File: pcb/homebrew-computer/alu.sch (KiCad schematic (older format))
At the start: 8 parts

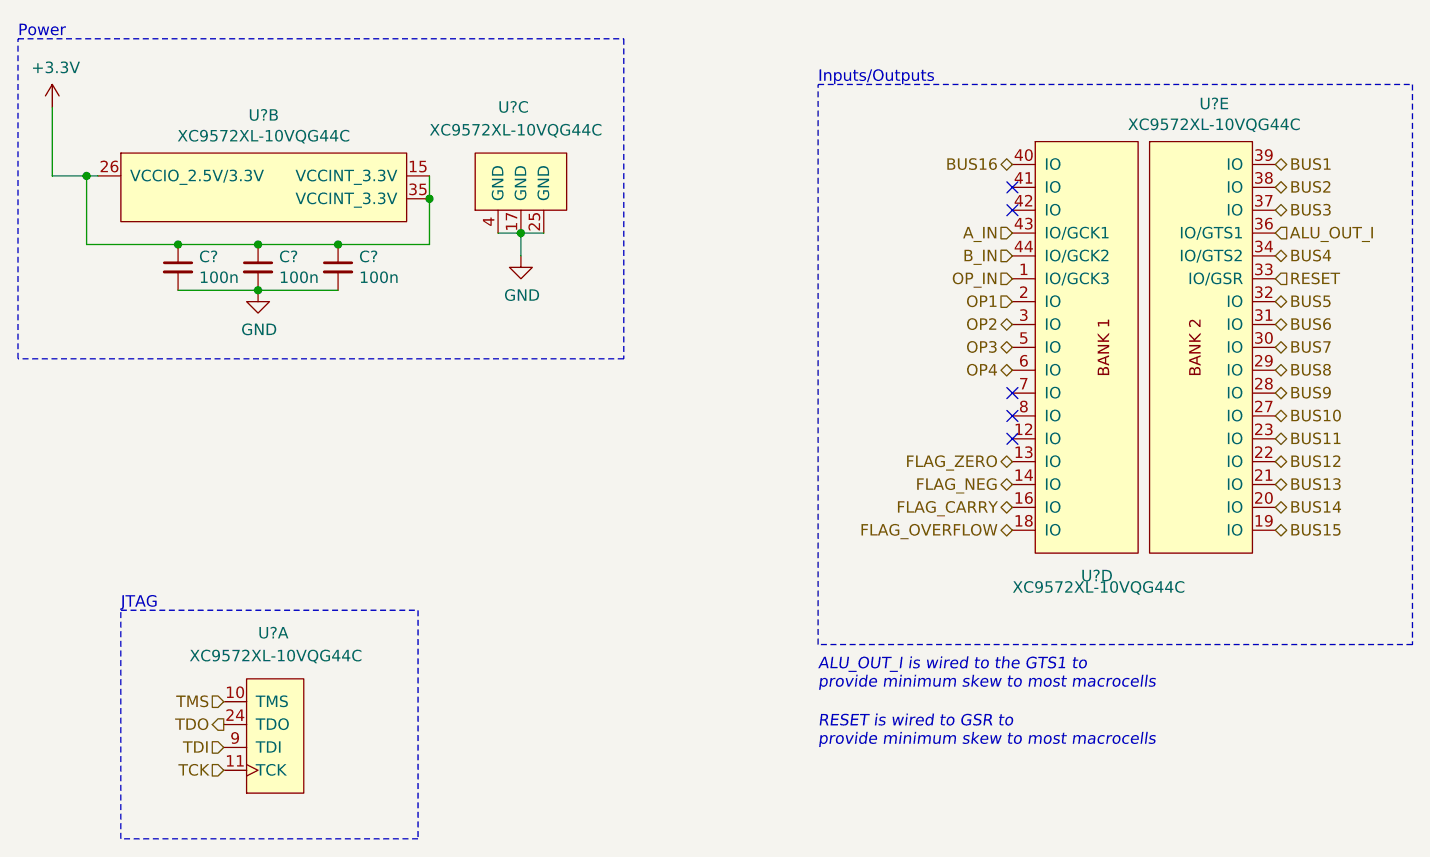
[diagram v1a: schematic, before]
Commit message: Start changing global labels with local labels
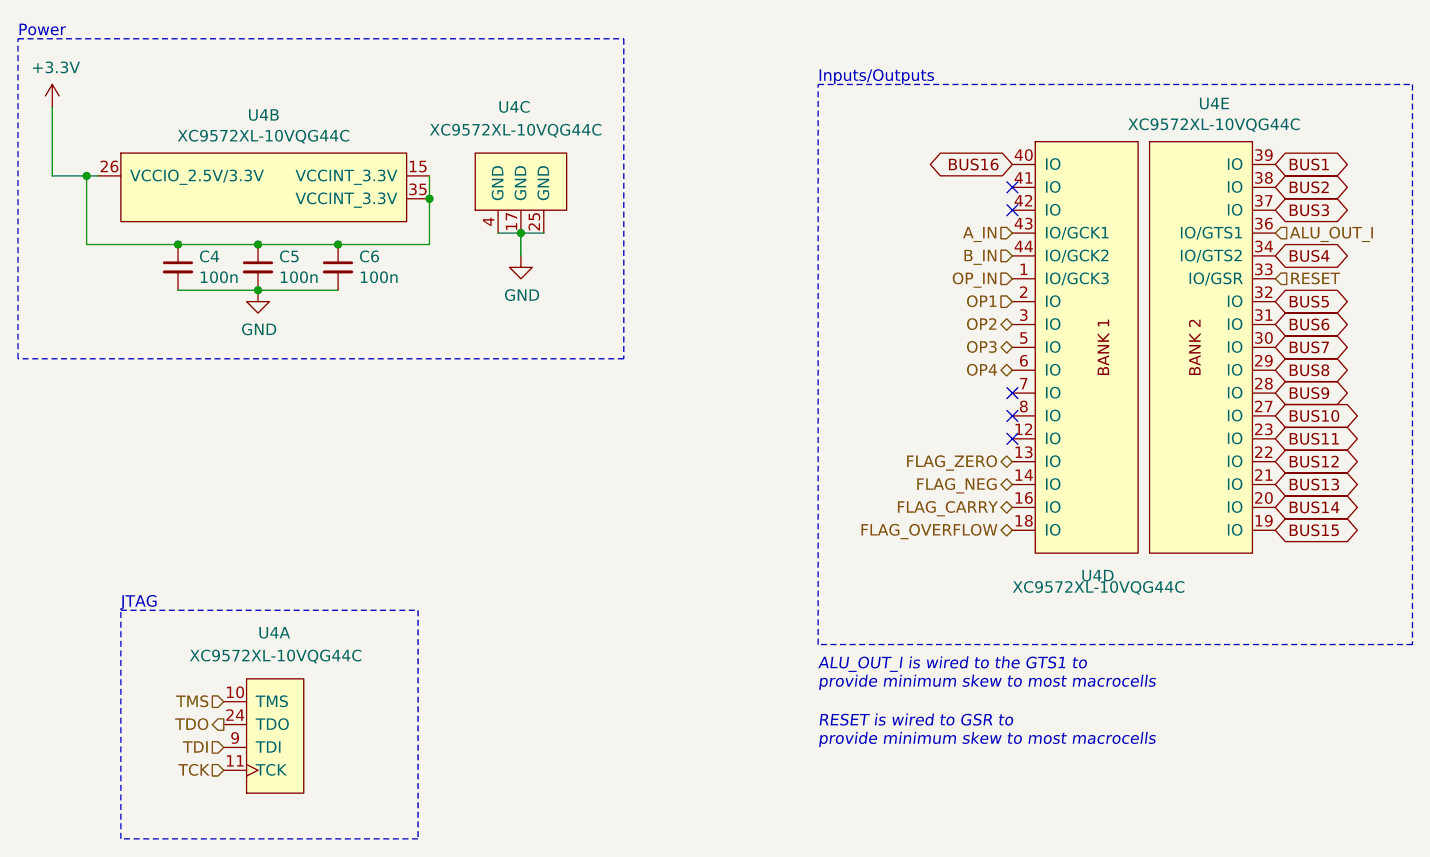
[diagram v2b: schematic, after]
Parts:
- gave numbers to parts that had none: 4
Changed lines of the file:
@@
 $Descr User 8661 5906
 encoding utf-8
-Sheet 2 7
+Sheet 5 7
 Title "Arithmetic and Logic Unit"
 Date "2020-10-24"
@@
 $EndComp
 $Comp
-L Device:C_Small C?
+L Device:C_Small C4
 U 1 1 5F8E42A8
 P 1700 1700
-F 0 "C?" H 1792 1746 50  0000 L CNN
+F 0 "C4" H 1792 1746 50  0000 L CNN
 F 1 "100n" H 1792 1655 50  0000 L CNN
 F 2 "" H 1700 1700 50  0001 C CNN
@@
 $EndComp
 $Comp
-L Device:C_Small C?
+L Device:C_Small C5
 U 1 1 5F8E4555
 P 2050 1700
-F 0 "C?" H 2142 1746 50  0000 L CNN
+F 0 "C5" H 2142 1746 50  0000 L CNN
 F 1 "100n" H 2142 1655 50  0000 L CNN
 F 2 "" H 2050 1700 50  0001 C CNN
@@
 $EndComp
 $Comp
-L Device:C_Small C?
+L Device:C_Small C6
 U 1 1 5F8E49E6
 P 2400 1700
-F 0 "C?" H 2492 1746 50  0000 L CNN
+F 0 "C6" H 2492 1746 50  0000 L CNN
 F 1 "100n" H 2492 1655 50  0000 L CNN
 F 2 "" H 2400 1700 50  0001 C CNN
@@
 Text HLabel 6500 1550 2    50   Input ~ 0
 ALU_OUT_I
-Text HLabel 6500 1250 2    50   3State ~ 0
-BUS1
-Text HLabel 6500 1350 2    50   3State ~ 0
-BUS2
-Text HLabel 6500 1450 2    50   3State ~ 0
-BUS3
-Text HLabel 6500 1650 2    50   3State ~ 0
-BUS4
-Text HLabel 6500 1850 2    50   3State ~ 0
-BUS5
-Text HLabel 6500 1950 2    50   3State ~ 0
-BUS6
-Text HLabel 6500 2050 2    50   3State ~ 0
-BUS7
-Text HLabel 6500 2150 2    50   3State ~ 0
-BUS8
-Text HLabel 6500 2250 2    50   3State ~ 0
-BUS9
-Text HLabel 6500 2350 2    50   3State ~ 0
-BUS10
-Text HLabel 6500 2450 2    50   3State ~ 0
-BUS11
-Text HLabel 6500 2550 2    50   3State ~ 0
-BUS12
-Text HLabel 6500 2650 2    50   3State ~ 0
-BUS13
-Text HLabel 6500 2750 2    50   3State ~ 0
-BUS14
-Text HLabel 6500 2850 2    50   3State ~ 0
-BUS15
-Text HLabel 5350 1250 0    50   3State ~ 0
-BUS16
 Text HLabel 5350 1550 0    50   Input ~ 0
 A_IN
@@
 OP_IN
 $Comp
-L XC9500XL:XC9572XL-10VQG44C U?
+L XC9500XL:XC9572XL-10VQG44C U4
 U 1 1 5F975DA0
 P 2100 4100
-F 0 "U?" H 2150 3300 50  0000 R CNN
+F 0 "U4" H 2150 3300 50  0000 R CNN
 F 1 "XC9572XL-10VQG44C" H 2450 3400 50  0000 R CNN
 F 2 "" H 2100 4100 50  0001 C CNN
@@
 $EndComp
 $Comp
-L XC9500XL:XC9572XL-10VQG44C U?
+L XC9500XL:XC9572XL-10VQG44C U4
 U 2 1 5F97A638
 P 2100 1100
-F 0 "U?" H 2075 1165 50  0000 C CNN
+F 0 "U4" H 2075 1165 50  0000 C CNN
 F 1 "XC9572XL-10VQG44C" H 2075 1074 50  0000 C CNN
 F 2 "" H 2100 1100 50  0001 C CNN
@@
 Connection ~ 2800 1400
 $Comp
-L XC9500XL:XC9572XL-10VQG44C U?
+L XC9500XL:XC9572XL-10VQG44C U4
 U 3 1 5F97D3D1
 P 2850 1350
-F 0 "U?" V 3200 1100 50  0000 R CNN
+F 0 "U4" V 3200 1100 50  0000 R CNN
 F 1 "XC9572XL-10VQG44C" V 3100 1400 50  0000 R CNN
 F 2 "" H 2850 1350 50  0001 C CNN
@@
 $EndComp
 $Comp
-L XC9500XL:XC9572XL-10VQG44C U?
+L XC9500XL:XC9572XL-10VQG44C U4
 U 4 1 5F982A18
 P 5700 1050
-F 0 "U?" H 5650 -950 50  0000 L CNN
+F 0 "U4" H 5650 -950 50  0000 L CNN
 F 1 "XC9572XL-10VQG44C" H 5350 -1000 50  0000 L CNN
 F 2 "" H 5700 1050 50  0001 C CNN
@@
 $EndComp
 $Comp
-L XC9500XL:XC9572XL-10VQG44C U?
+L XC9500XL:XC9572XL-10VQG44C U4
 U 5 1 5F987E07
 P 6200 1050
-F 0 "U?" H 6233 1115 50  0000 C CNN
+F 0 "U4" H 6233 1115 50  0000 C CNN
 F 1 "XC9572XL-10VQG44C" H 6233 1024 50  0000 C CNN
 F 2 "" H 6200 1050 50  0001 C CNN
@@
 Text Notes 4500 3800 0    50   Italic 0
 RESET is wired to GSR to\nprovide minimum skew to most macrocells
+Text GLabel 5350 1250 0    50   3State ~ 0
+BUS16
+Text GLabel 6500 2850 2    50   3State ~ 0
+BUS15
+Text GLabel 6500 2750 2    50   3State ~ 0
+BUS14
+Text GLabel 6500 2650 2    50   3State ~ 0
+BUS13
+Text GLabel 6500 2550 2    50   3State ~ 0
+BUS12
+Text GLabel 6500 2450 2    50   3State ~ 0
+BUS11
+Text GLabel 6500 2350 2    50   3State ~ 0
+BUS10
+Text GLabel 6500 2250 2    50   3State ~ 0
+BUS9
+Text GLabel 6500 2150 2    50   3State ~ 0
+BUS8
+Text GLabel 6500 2050 2    50   3State ~ 0
+BUS7
+Text GLabel 6500 1950 2    50   3State ~ 0
+BUS6
+Text GLabel 6500 1850 2    50   3State ~ 0
+BUS5
+Text GLabel 6500 1650 2    50   3State ~ 0
+BUS4
+Text GLabel 6500 1450 2    50   3State ~ 0
+BUS3
+Text GLabel 6500 1350 2    50   3State ~ 0
+BUS2
+Text GLabel 6500 1250 2    50   3State ~ 0
+BUS1
 $EndSCHEMATC

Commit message: Start working on the pcb layout
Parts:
- C4, C5, C6: footprint (none) -> Capacitor_SMD:C_0402_1005Metric_Pad0.74x0.62mm_HandSolder
- U4: footprint (none) -> Package_QFP:VQFP-44; symbol XC9500XL:XC9572XL-10VQG44C -> homebrew-computer-rescue:XC9572XL-10VQG44C-XC9500XL
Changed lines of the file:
@@
 $Descr User 8661 5906
 encoding utf-8
-Sheet 5 7
+Sheet 6 7
 Title "Arithmetic and Logic Unit"
 Date "2020-10-24"
@@
 U 1 1 5F8DE7DB
 P 1150 1000
+AR Path="/5F8B5CB7/5F8DE7DB" Ref="#PWR0109"  Part="1"
+AR Path="/5FA0F66F/5F8DE7DB" Ref="#PWR?"  Part="1"
+AR Path="/5FA0FB14/5F8DE7DB" Ref="#PWR?"  Part="1"
+AR Path="/5FA0FEFC/5F8DE7DB" Ref="#PWR?"  Part="1"
 F 0 "#PWR0109" H 1150 850 50  0001 C CNN
 F 1 "+3.3V" H 1165 1173 50  0000 C CNN
@@
 U 1 1 5F8DF382
 P 3200 1650
+AR Path="/5F8B5CB7/5F8DF382" Ref="#PWR0110"  Part="1"
+AR Path="/5FA0F66F/5F8DF382" Ref="#PWR?"  Part="1"
+AR Path="/5FA0FB14/5F8DF382" Ref="#PWR?"  Part="1"
+AR Path="/5FA0FEFC/5F8DF382" Ref="#PWR?"  Part="1"
 F 0 "#PWR0110" H 3200 1400 50  0001 C CNN
 F 1 "GND" H 3205 1477 50  0000 C CNN
@@
 U 1 1 5F8E42A8
 P 1700 1700
+AR Path="/5F8B5CB7/5F8E42A8" Ref="C4"  Part="1"
+AR Path="/5FA0F66F/5F8E42A8" Ref="C?"  Part="1"
+AR Path="/5FA0FB14/5F8E42A8" Ref="C?"  Part="1"
+AR Path="/5FA0FEFC/5F8E42A8" Ref="C?"  Part="1"
 F 0 "C4" H 1792 1746 50  0000 L CNN
 F 1 "100n" H 1792 1655 50  0000 L CNN
-F 2 "" H 1700 1700 50  0001 C CNN
+F 2 "Capacitor_SMD:C_0402_1005Metric_Pad0.74x0.62mm_HandSolder" H 1700 1700 50  0001 C CNN
 F 3 "~" H 1700 1700 50  0001 C CNN
 	1    1700 1700
@@
 U 1 1 5F8E4555
 P 2050 1700
+AR Path="/5F8B5CB7/5F8E4555" Ref="C5"  Part="1"
+AR Path="/5FA0F66F/5F8E4555" Ref="C?"  Part="1"
+AR Path="/5FA0FB14/5F8E4555" Ref="C?"  Part="1"
+AR Path="/5FA0FEFC/5F8E4555" Ref="C?"  Part="1"
 F 0 "C5" H 2142 1746 50  0000 L CNN
 F 1 "100n" H 2142 1655 50  0000 L CNN
-F 2 "" H 2050 1700 50  0001 C CNN
+F 2 "Capacitor_SMD:C_0402_1005Metric_Pad0.74x0.62mm_HandSolder" H 2050 1700 50  0001 C CNN
 F 3 "~" H 2050 1700 50  0001 C CNN
 	1    2050 1700
@@
 U 1 1 5F8E49E6
 P 2400 1700
+AR Path="/5F8B5CB7/5F8E49E6" Ref="C6"  Part="1"
+AR Path="/5FA0F66F/5F8E49E6" Ref="C?"  Part="1"
+AR Path="/5FA0FB14/5F8E49E6" Ref="C?"  Part="1"
+AR Path="/5FA0FEFC/5F8E49E6" Ref="C?"  Part="1"
 F 0 "C6" H 2492 1746 50  0000 L CNN
 F 1 "100n" H 2492 1655 50  0000 L CNN
-F 2 "" H 2400 1700 50  0001 C CNN
+F 2 "Capacitor_SMD:C_0402_1005Metric_Pad0.74x0.62mm_HandSolder" H 2400 1700 50  0001 C CNN
 F 3 "~" H 2400 1700 50  0001 C CNN
 	1    2400 1700
@@
 	2800 1600 2400 1600
 Connection ~ 2400 1600
-Wire Wire Line
-	1700 1800 2050 1800
-Connection ~ 2050 1800
-Wire Wire Line
-	2050 1800 2400 1800
 Connection ~ 3200 1550
 Wire Wire Line
@@
 L power:GND #PWR0111
 U 1 1 5F8EE955
-P 2050 1800
-F 0 "#PWR0111" H 2050 1550 50  0001 C CNN
-F 1 "GND" H 2055 1627 50  0000 C CNN
-F 2 "" H 2050 1800 50  0001 C CNN
-F 3 "" H 2050 1800 50  0001 C CNN
-	1    2050 1800
+P 2050 1850
+AR Path="/5F8B5CB7/5F8EE955" Ref="#PWR0111"  Part="1"
+AR Path="/5FA0F66F/5F8EE955" Ref="#PWR?"  Part="1"
+AR Path="/5FA0FB14/5F8EE955" Ref="#PWR?"  Part="1"
+AR Path="/5FA0FEFC/5F8EE955" Ref="#PWR?"  Part="1"
+F 0 "#PWR0111" H 2050 1600 50  0001 C CNN
+F 1 "GND" H 2055 1677 50  0000 C CNN
+F 2 "" H 2050 1850 50  0001 C CNN
+F 3 "" H 2050 1850 50  0001 C CNN
+	1    2050 1850
 	1    0    0    -1
 $EndComp
@@
 OP_IN
 $Comp
-L XC9500XL:XC9572XL-10VQG44C U4
+L homebrew-computer-rescue:XC9572XL-10VQG44C-XC9500XL U4
 U 1 1 5F975DA0
 P 2100 4100
+AR Path="/5F8B5CB7/5F975DA0" Ref="U4"  Part="1"
+AR Path="/5FA0F66F/5F975DA0" Ref="U?"  Part="1"
+AR Path="/5FA0FB14/5F975DA0" Ref="U?"  Part="1"
+AR Path="/5FA0FEFC/5F975DA0" Ref="U?"  Part="1"
 F 0 "U4" H 2150 3300 50  0000 R CNN
 F 1 "XC9572XL-10VQG44C" H 2450 3400 50  0000 R CNN
-F 2 "" H 2100 4100 50  0001 C CNN
+F 2 "Package_QFP:VQFP-44" H 2100 4100 50  0001 C CNN
 F 3 "" H 2100 4100 50  0001 C CNN
 	1    2100 4100
@@
 $EndComp
 $Comp
-L XC9500XL:XC9572XL-10VQG44C U4
+L homebrew-computer-rescue:XC9572XL-10VQG44C-XC9500XL U4
 U 2 1 5F97A638
 P 2100 1100
+AR Path="/5F8B5CB7/5F97A638" Ref="U4"  Part="2"
+AR Path="/5FA0F66F/5F97A638" Ref="U?"  Part="2"
+AR Path="/5FA0FB14/5F97A638" Ref="U?"  Part="2"
+AR Path="/5FA0FEFC/5F97A638" Ref="U?"  Part="2"
 F 0 "U4" H 2075 1165 50  0000 C CNN
 F 1 "XC9572XL-10VQG44C" H 2075 1074 50  0000 C CNN
-F 2 "" H 2100 1100 50  0001 C CNN
+F 2 "Package_QFP:VQFP-44" H 2100 1100 50  0001 C CNN
 F 3 "" H 2100 1100 50  0001 C CNN
 	2    2100 1100
@@
 Connection ~ 2800 1400
 $Comp
-L XC9500XL:XC9572XL-10VQG44C U4
+L homebrew-computer-rescue:XC9572XL-10VQG44C-XC9500XL U4
 U 3 1 5F97D3D1
 P 2850 1350
+AR Path="/5F8B5CB7/5F97D3D1" Ref="U4"  Part="3"
+AR Path="/5FA0F66F/5F97D3D1" Ref="U?"  Part="3"
+AR Path="/5FA0FB14/5F97D3D1" Ref="U?"  Part="3"
+AR Path="/5FA0FEFC/5F97D3D1" Ref="U?"  Part="3"
 F 0 "U4" V 3200 1100 50  0000 R CNN
 F 1 "XC9572XL-10VQG44C" V 3100 1400 50  0000 R CNN
-F 2 "" H 2850 1350 50  0001 C CNN
+F 2 "Package_QFP:VQFP-44" H 2850 1350 50  0001 C CNN
 F 3 "" H 2850 1350 50  0001 C CNN
 	3    2850 1350
@@
 $EndComp
 $Comp
-L XC9500XL:XC9572XL-10VQG44C U4
+L homebrew-computer-rescue:XC9572XL-10VQG44C-XC9500XL U4
 U 4 1 5F982A18
 P 5700 1050
+AR Path="/5F8B5CB7/5F982A18" Ref="U4"  Part="4"
+AR Path="/5FA0F66F/5F982A18" Ref="U?"  Part="4"
+AR Path="/5FA0FB14/5F982A18" Ref="U?"  Part="4"
+AR Path="/5FA0FEFC/5F982A18" Ref="U?"  Part="4"
 F 0 "U4" H 5650 -950 50  0000 L CNN
 F 1 "XC9572XL-10VQG44C" H 5350 -1000 50  0000 L CNN
-F 2 "" H 5700 1050 50  0001 C CNN
+F 2 "Package_QFP:VQFP-44" H 5700 1050 50  0001 C CNN
 F 3 "" H 5700 1050 50  0001 C CNN
 	4    5700 1050
@@
 $EndComp
 $Comp
-L XC9500XL:XC9572XL-10VQG44C U4
+L homebrew-computer-rescue:XC9572XL-10VQG44C-XC9500XL U4
 U 5 1 5F987E07
 P 6200 1050
+AR Path="/5F8B5CB7/5F987E07" Ref="U4"  Part="5"
+AR Path="/5FA0F66F/5F987E07" Ref="U?"  Part="5"
+AR Path="/5FA0FB14/5F987E07" Ref="U?"  Part="5"
+AR Path="/5FA0FEFC/5F987E07" Ref="U?"  Part="5"
 F 0 "U4" H 6233 1115 50  0000 C CNN
 F 1 "XC9572XL-10VQG44C" H 6233 1024 50  0000 C CNN
-F 2 "" H 6200 1050 50  0001 C CNN
+F 2 "Package_QFP:VQFP-44" H 6200 1050 50  0001 C CNN
 F 3 "" H 6200 1050 50  0001 C CNN
 	5    6200 1050
@@
 Text GLabel 6500 1250 2    50   3State ~ 0
 BUS1
+Wire Wire Line
+	1700 1800 2050 1800
+Wire Wire Line
+	2050 1850 2050 1800
+Connection ~ 2050 1800
+Wire Wire Line
+	2050 1800 2400 1800
 $EndSCHEMATC

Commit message: Keep working on the layout
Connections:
- net ALU_OUT_I: now also U4.34 (IO/GTS2); no longer U4.36 (IO/GTS1)
- net A_IN: now also U4.32 (IO); no longer U4.43 (IO/GCK1)
- net BUS1: now also U4.36 (IO/GTS1); no longer U4.39 (IO)
- net BUS10: now also U4.1 (IO/GCK3); no longer U4.27 (IO)
- net BUS11: now also U4.2 (IO); no longer U4.23 (IO)
- net BUS12: now also U4.3 (IO); no longer U4.22 (IO)
- net BUS13: now also U4.5 (IO); no longer U4.21 (IO)
- net BUS14: now also U4.6 (IO); no longer U4.20 (IO)
- net BUS15: now also U4.7 (IO); no longer U4.19 (IO)
- net BUS16: now also U4.8 (IO); no longer U4.40 (IO)
- net BUS2: now also U4.37 (IO); no longer U4.38 (IO)
- net BUS3: now also U4.38 (IO); no longer U4.37 (IO)
- net BUS4: now also U4.39 (IO); no longer U4.34 (IO/GTS2)
- net BUS5: now also U4.40 (IO); no longer U4.32 (IO)
- net BUS6: now also U4.41 (IO); no longer U4.31 (IO)
- net BUS7: now also U4.42 (IO); no longer U4.30 (IO)
- net BUS8: now also U4.43 (IO/GCK1); no longer U4.29 (IO)
- net BUS9: now also U4.44 (IO/GCK2); no longer U4.28 (IO)
- net B_IN: now also U4.31 (IO); no longer U4.44 (IO/GCK2)
- net OP1: now also U4.29 (IO); no longer U4.2 (IO)
- net OP2: now also U4.28 (IO); no longer U4.3 (IO)
- net OP3: now also U4.27 (IO); no longer U4.5 (IO)
- net OP4: now also U4.23 (IO); no longer U4.6 (IO)
- net OP_IN: now also U4.30 (IO); no longer U4.1 (IO/GCK3)
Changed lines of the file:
@@
 Text Notes 1450 3200 0    50   ~ 0
 JTAG
-Text HLabel 5350 1850 0    50   Input ~ 0
+Text HLabel 6500 2150 2    50   Input ~ 0
 OP1
-Text HLabel 5350 1950 0    50   3State ~ 0
+Text HLabel 6500 2250 2    50   3State ~ 0
 OP2
-Text HLabel 5350 2050 0    50   3State ~ 0
+Text HLabel 6500 2350 2    50   3State ~ 0
 OP3
-Text HLabel 5350 2150 0    50   3State ~ 0
+Text HLabel 6500 2450 2    50   3State ~ 0
 OP4
-Text HLabel 5350 2550 0    50   3State ~ 0
-FLAG_ZERO
-Text HLabel 5350 2650 0    50   3State ~ 0
-FLAG_NEG
-Text HLabel 5350 2750 0    50   3State ~ 0
-FLAG_CARRY
-Text HLabel 5350 2850 0    50   3State ~ 0
-FLAG_OVERFLOW
-NoConn ~ 5350 1350
-NoConn ~ 5350 1450
-NoConn ~ 5350 2250
-NoConn ~ 5350 2450
 Wire Notes Line
 	4500 900  7100 900
@@
 Text Notes 4500 900  0    50   ~ 0
 Inputs/Outputs
-Text HLabel 6500 1550 2    50   Input ~ 0
+Text HLabel 6500 1650 2    50   Input ~ 0
 ALU_OUT_I
-Text HLabel 5350 1550 0    50   Input ~ 0
+Text HLabel 6500 1850 2    50   Input ~ 0
 A_IN
-Text HLabel 5350 1650 0    50   Input ~ 0
+Text HLabel 6500 1950 2    50   Input ~ 0
 B_IN
-Text HLabel 5350 1750 0    50   Input ~ 0
+Text HLabel 6500 2050 2    50   Input ~ 0
 OP_IN
 $Comp
@@
 Text HLabel 6500 1750 2    50   Input ~ 0
 RESET
-NoConn ~ 5350 2350
 Text Notes 4500 3550 0    50   Italic 0
 ALU_OUT_I is wired to the GTS1 to\nprovide minimum skew to most macrocells
 Text Notes 4500 3800 0    50   Italic 0
 RESET is wired to GSR to\nprovide minimum skew to most macrocells
+Text GLabel 5350 2350 0    50   3State ~ 0
+BUS16
+Text GLabel 5350 2250 0    50   3State ~ 0
+BUS15
+Text GLabel 5350 2150 0    50   3State ~ 0
+BUS14
+Text GLabel 5350 2050 0    50   3State ~ 0
+BUS13
+Text GLabel 5350 1950 0    50   3State ~ 0
+BUS12
+Text GLabel 5350 1850 0    50   3State ~ 0
+BUS11
+Text GLabel 5350 1750 0    50   3State ~ 0
+BUS10
+Text GLabel 5350 1650 0    50   3State ~ 0
+BUS9
+Text GLabel 5350 1550 0    50   3State ~ 0
+BUS8
+Text GLabel 5350 1450 0    50   3State ~ 0
+BUS7
+Text GLabel 5350 1350 0    50   3State ~ 0
+BUS6
 Text GLabel 5350 1250 0    50   3State ~ 0
-BUS16
-Text GLabel 6500 2850 2    50   3State ~ 0
-BUS15
-Text GLabel 6500 2750 2    50   3State ~ 0
-BUS14
-Text GLabel 6500 2650 2    50   3State ~ 0
-BUS13
-Text GLabel 6500 2550 2    50   3State ~ 0
-BUS12
-Text GLabel 6500 2450 2    50   3State ~ 0
-BUS11
-Text GLabel 6500 2350 2    50   3State ~ 0
-BUS10
-Text GLabel 6500 2250 2    50   3State ~ 0
-BUS9
-Text GLabel 6500 2150 2    50   3State ~ 0
-BUS8
-Text GLabel 6500 2050 2    50   3State ~ 0
-BUS7
-Text GLabel 6500 1950 2    50   3State ~ 0
-BUS6
-Text GLabel 6500 1850 2    50   3State ~ 0
 BUS5
-Text GLabel 6500 1650 2    50   3State ~ 0
+Text GLabel 6500 1250 2    50   3State ~ 0
 BUS4
+Text GLabel 6500 1350 2    50   3State ~ 0
+BUS3
 Text GLabel 6500 1450 2    50   3State ~ 0
-BUS3
-Text GLabel 6500 1350 2    50   3State ~ 0
 BUS2
-Text GLabel 6500 1250 2    50   3State ~ 0
+Text GLabel 6500 1550 2    50   3State ~ 0
 BUS1
 Wire Wire Line
@@
 Wire Wire Line
 	2050 1800 2400 1800
+NoConn ~ 6500 2850
+NoConn ~ 6500 2750
+NoConn ~ 6500 2650
+NoConn ~ 6500 2550
+NoConn ~ 5350 2450
+Text HLabel 5350 2850 0    50   3State ~ 0
+FLAG_OVERFLOW
+Text HLabel 5350 2750 0    50   3State ~ 0
+FLAG_CARRY
+Text HLabel 5350 2650 0    50   3State ~ 0
+FLAG_NEG
+Text HLabel 5350 2550 0    50   3State ~ 0
+FLAG_ZERO
 $EndSCHEMATC

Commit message: Keep working on the layout
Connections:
- net A_IN: now also U4.27 (IO); no longer U4.32 (IO)
- net B_IN: now also U4.23 (IO); no longer U4.31 (IO)
- net FLAG_CARRY: now also U4.14 (IO); no longer U4.16 (IO)
- net FLAG_NEG: now also U4.13 (IO); no longer U4.14 (IO)
- net FLAG_OVERFLOW: now also U4.16 (IO); no longer U4.18 (IO)
- net FLAG_ZERO: now also U4.12 (IO); no longer U4.13 (IO)
- net OP1: now also U4.22 (IO); no longer U4.29 (IO)
- net OP2: now also U4.21 (IO); no longer U4.28 (IO)
- net OP3: now also U4.20 (IO); no longer U4.27 (IO)
- net OP4: now also U4.19 (IO); no longer U4.23 (IO)
- net OP_IN: now also U4.18 (IO); no longer U4.30 (IO)
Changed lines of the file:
@@
 Text Notes 1450 3200 0    50   ~ 0
 JTAG
-Text HLabel 6500 2150 2    50   Input ~ 0
+Text HLabel 6500 2550 2    50   Input ~ 0
 OP1
-Text HLabel 6500 2250 2    50   3State ~ 0
+Text HLabel 6500 2650 2    50   3State ~ 0
 OP2
-Text HLabel 6500 2350 2    50   3State ~ 0
+Text HLabel 6500 2750 2    50   3State ~ 0
 OP3
-Text HLabel 6500 2450 2    50   3State ~ 0
+Text HLabel 6500 2850 2    50   3State ~ 0
 OP4
 Wire Notes Line
@@
 Text HLabel 6500 1650 2    50   Input ~ 0
 ALU_OUT_I
-Text HLabel 6500 1850 2    50   Input ~ 0
+Text HLabel 6500 2350 2    50   Input ~ 0
 A_IN
-Text HLabel 6500 1950 2    50   Input ~ 0
+Text HLabel 6500 2450 2    50   Input ~ 0
 B_IN
-Text HLabel 6500 2050 2    50   Input ~ 0
+Text HLabel 5350 2850 0    50   Input ~ 0
 OP_IN
 $Comp
@@
 Wire Wire Line
 	2050 1800 2400 1800
-NoConn ~ 6500 2850
-NoConn ~ 6500 2750
-NoConn ~ 6500 2650
-NoConn ~ 6500 2550
-NoConn ~ 5350 2450
-Text HLabel 5350 2850 0    50   3State ~ 0
+Text HLabel 5350 2750 0    50   3State ~ 0
 FLAG_OVERFLOW
-Text HLabel 5350 2750 0    50   3State ~ 0
+Text HLabel 5350 2650 0    50   3State ~ 0
 FLAG_CARRY
-Text HLabel 5350 2650 0    50   3State ~ 0
+Text HLabel 5350 2550 0    50   3State ~ 0
 FLAG_NEG
-Text HLabel 5350 2550 0    50   3State ~ 0
+Text HLabel 5350 2450 0    50   3State ~ 0
 FLAG_ZERO
+NoConn ~ 6500 2250
+NoConn ~ 6500 2150
+NoConn ~ 6500 2050
+NoConn ~ 6500 1950
+NoConn ~ 6500 1850
 $EndSCHEMATC
